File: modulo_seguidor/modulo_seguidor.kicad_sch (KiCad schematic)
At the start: 28 parts, among them J1 Battery, J2 Motor A Entradas, J4 Motor IZQ Arduino OUTPUT, J6 puerto sensores, M1 Motor_IZQ, M2 Motor_DER, SW1 SW_Push, SW2 SW_Nidec_CAS-120A1, U1 LM7806_TO220, U2 L298N

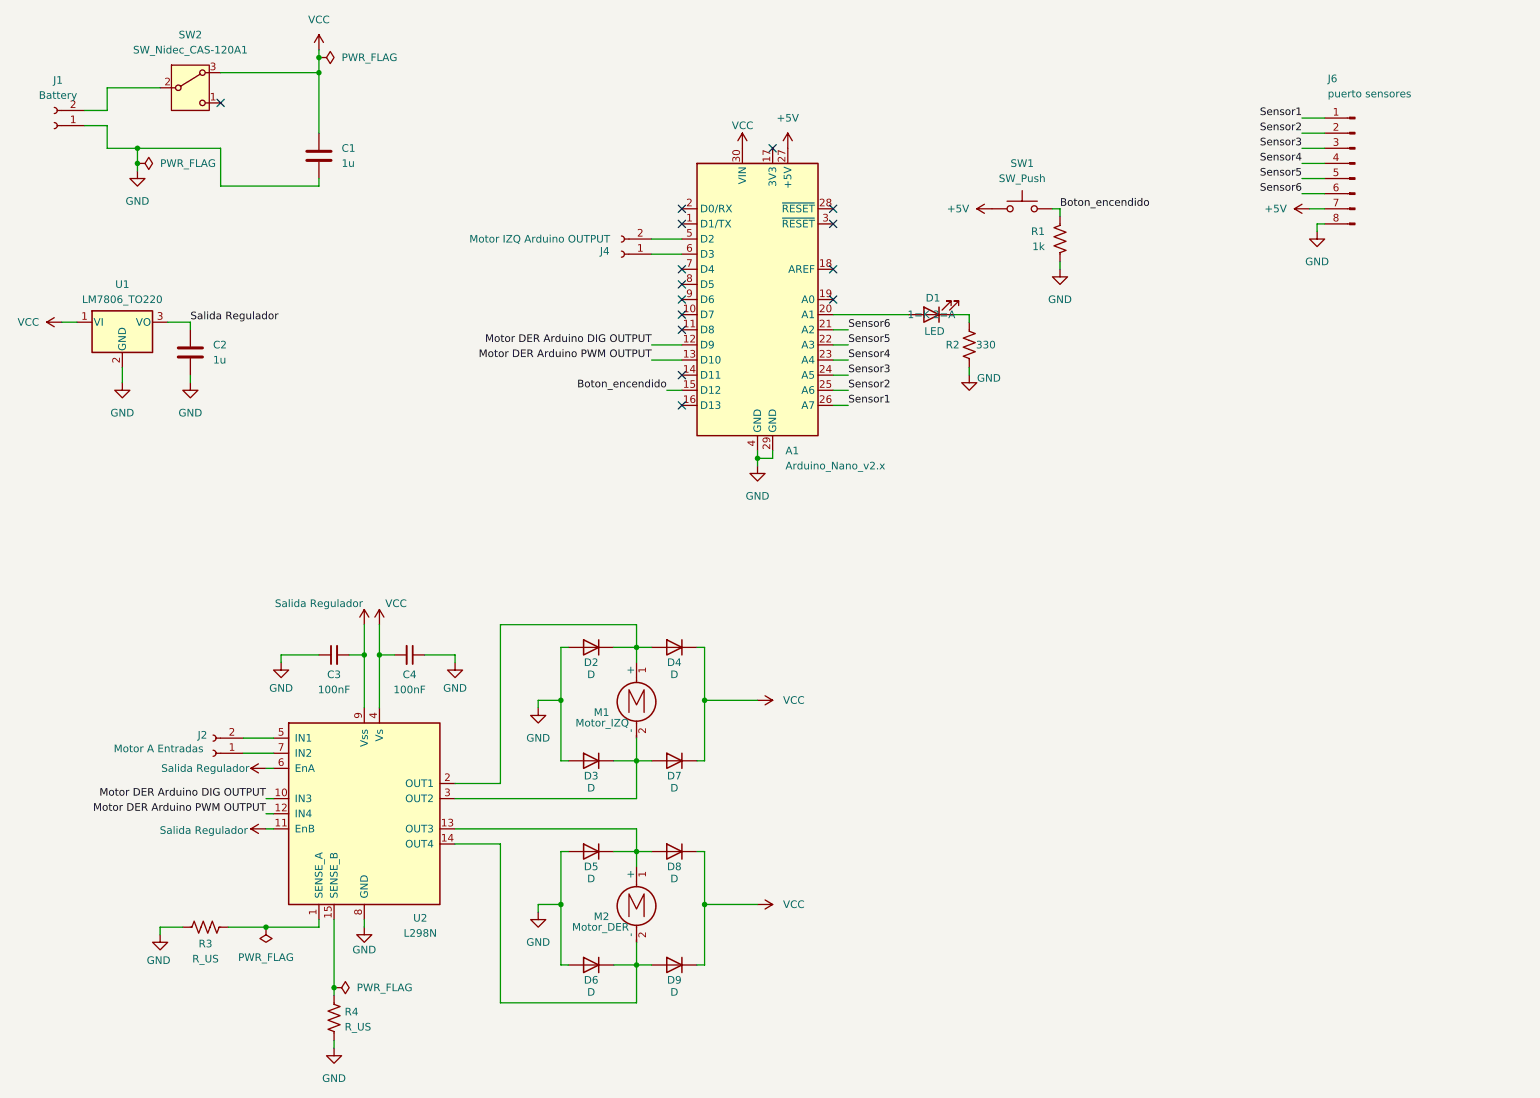
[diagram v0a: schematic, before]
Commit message: Cambios placa sensor
Se asignaron pines distintos para los motores, se movieron  varias cosas y está el intento de sumar el modulo hm-10
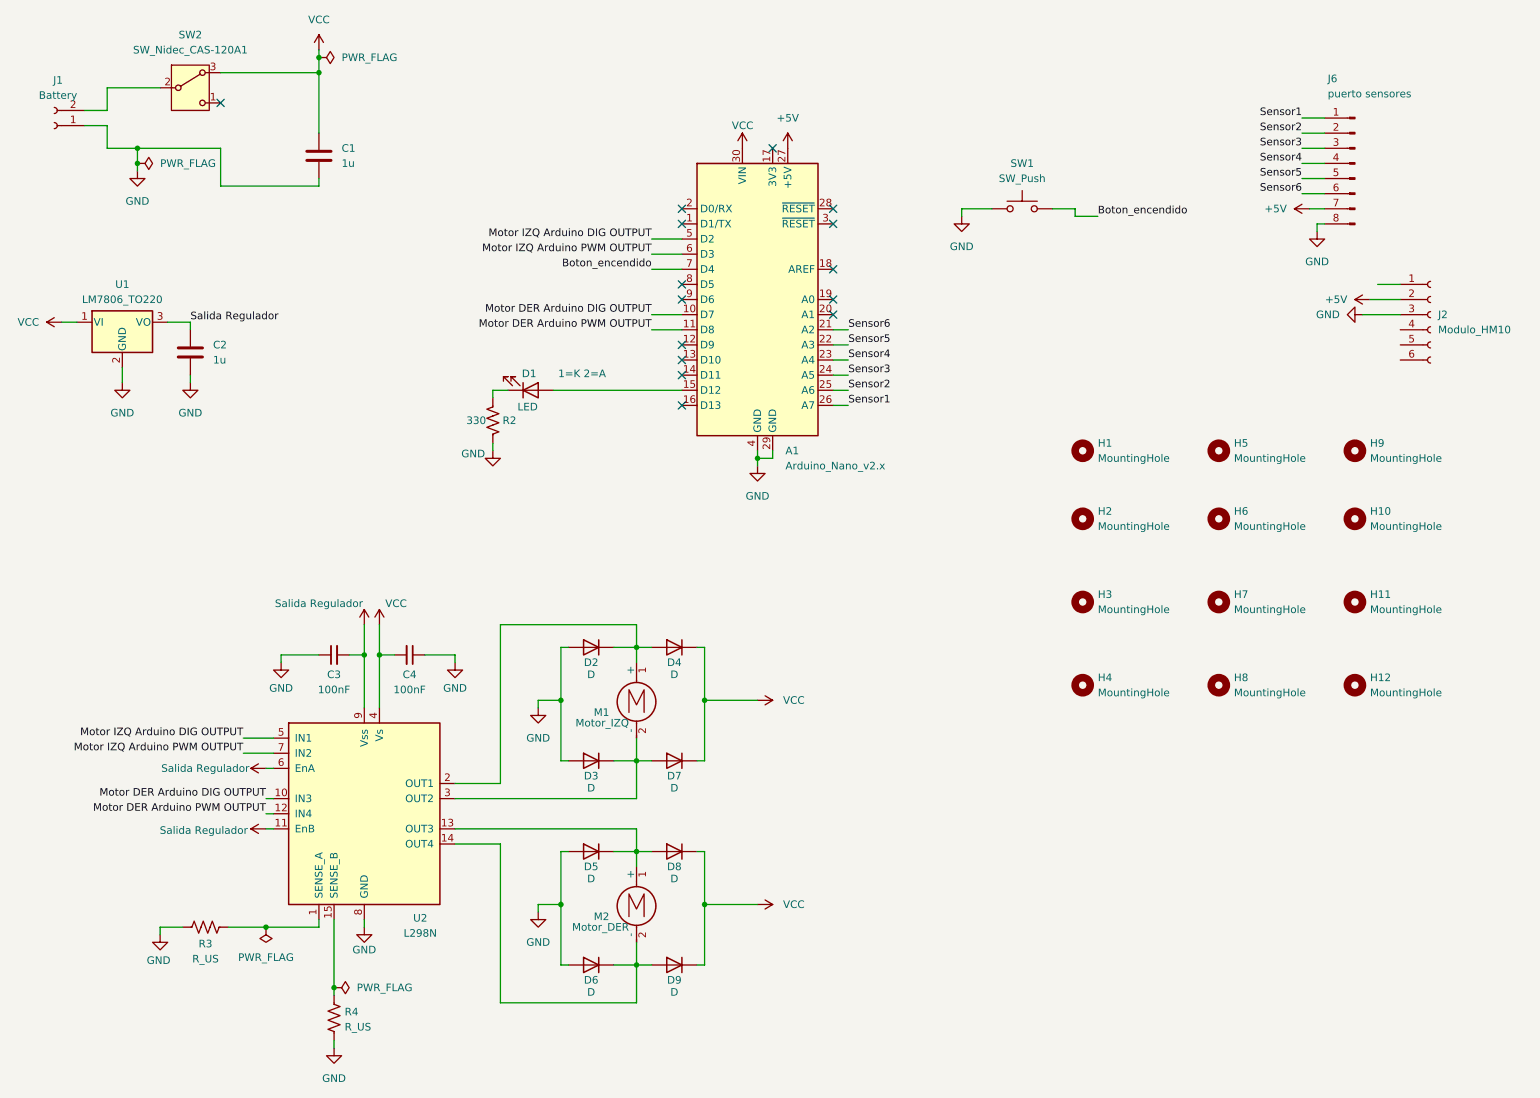
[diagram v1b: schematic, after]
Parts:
- removed J2: Motor A Entradas, Connector_Molex:Molex_KK-254_AE-6410-02A_1x02_P2.54mm_Vertical, symbol Connector:Conn_01x02_Socket
- removed J4: Motor IZQ Arduino OUTPUT, Connector_Molex:Molex_KK-254_AE-6410-02A_1x02_P2.54mm_Vertical, symbol Connector:Conn_01x02_Socket
- removed R1: 1k, Resistor_SMD:R_1206_3216Metric_Pad1.30x1.75mm_HandSolder, symbol Device:R_US
- added H1, H10, H11, H12, H2, H3, H4, H5, H6, H7, H8, H9: MountingHole, MountingHole:MountingHole_3.2mm_M3, symbol Mechanical:MountingHole
- added J2: Modulo_HM10, symbol Connector:Conn_01x06_Socket
- J6: footprint Connector_PinHeader_2.54mm:PinHeader_1x08_P2.54mm_Horizontal -> Connector_PinSocket_2.54mm:PinSocket_1x08_P2.54mm_Horizontal
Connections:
- net +5V: now also J2.2 (Pin_2); no longer SW1.1
- net Boton_encendido: now also A1.7 (D4); no longer A1.15 (D12)
- net GND: now also SW1.1, J2.3 (Pin_3)
- net Motor DER Arduino DIG OUTPUT: now also A1.10 (D7); no longer A1.12 (D9)
- net Motor DER Arduino PWM OUTPUT: now also A1.11 (D8); no longer A1.13 (D10)
- net Motor IZQ Arduino PWM OUTPUT: now reaches U2.7 (IN2)
- net Motor IZQ Arduino PWM OUTPUT: now also A1.6 (D3)
- net Motor IZQ Arduino DIG OUTPUT: now reaches U2.5 (IN1)
- net Motor IZQ Arduino DIG OUTPUT: now also A1.5 (D2)
- net at D1.2 (A): now also A1.15 (D12); no longer A1.20 (A1)
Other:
- moved on the sheet: D1, R2

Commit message: Actualizaciones de la ultima placa del seguidor
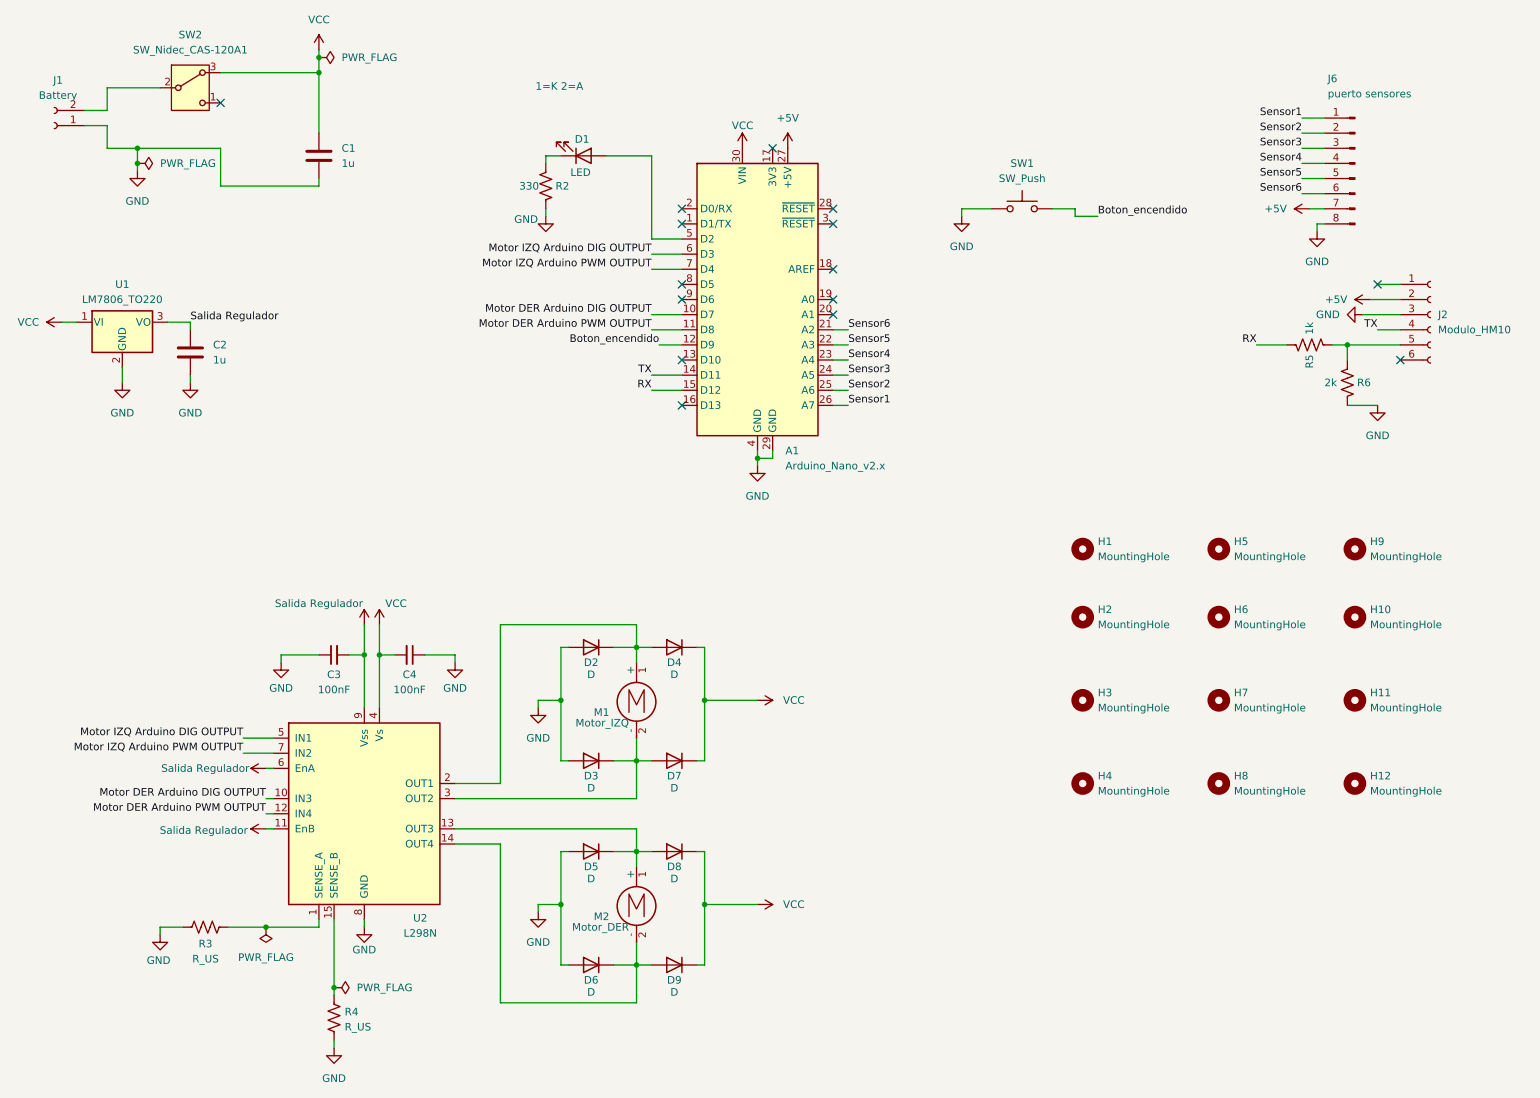
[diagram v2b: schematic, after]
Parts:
- added R5: 1k, Resistor_SMD:R_1206_3216Metric_Pad1.30x1.75mm_HandSolder, symbol Device:R_US
- added R6: 2k, Resistor_SMD:R_1206_3216Metric_Pad1.30x1.75mm_HandSolder, symbol Device:R_US
- J2: footprint (none) -> Connector_PinSocket_2.54mm:PinSocket_1x06_P2.54mm_Vertical
- R3, R4: footprint Resistor_SMD:R_0805_2012Metric_Pad1.20x1.40mm_HandSolder -> Resistor_THT:R_Axial_DIN0207_L6.3mm_D2.5mm_P10.16mm_Horizontal
- SW1: footprint Button_Switch_THT:SW_PUSH_6mm -> Button_Switch_THT:SW_PUSH_6mm_H5mm
- SW2: footprint Converter_DCDC:Converter_DCDC_TRACO_TSR2-xxxx_THT -> Connector_Wire:SolderWire-0.5sqmm_1x03_P4.6mm_D0.9mm_OD2.1mm
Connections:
- net Boton_encendido: now also A1.12 (D9); no longer A1.7 (D4)
- net GND: now also R6.2
- net Motor IZQ Arduino DIG OUTPUT: now also A1.6 (D3); no longer A1.5 (D2)
- net Motor IZQ Arduino PWM OUTPUT: now also A1.7 (D4); no longer A1.6 (D3)
- net TX: now reaches J2.4 (Pin_4)
- net TX: now also A1.14 (D11)
- net at J2.5 (Pin_5): now also R5.1, R6.1
- net at D1.2 (A): now also A1.5 (D2); no longer A1.15 (D12)
- new net RX: A1.15 (D12), R5.2
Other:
- moved on the sheet: D1, H1, H10, H11, H12, H2, H3, H4, H5, H6, H7, H8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
